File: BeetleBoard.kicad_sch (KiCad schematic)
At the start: 1 part, among them U1 XIAO-ESP32-C6-SMD

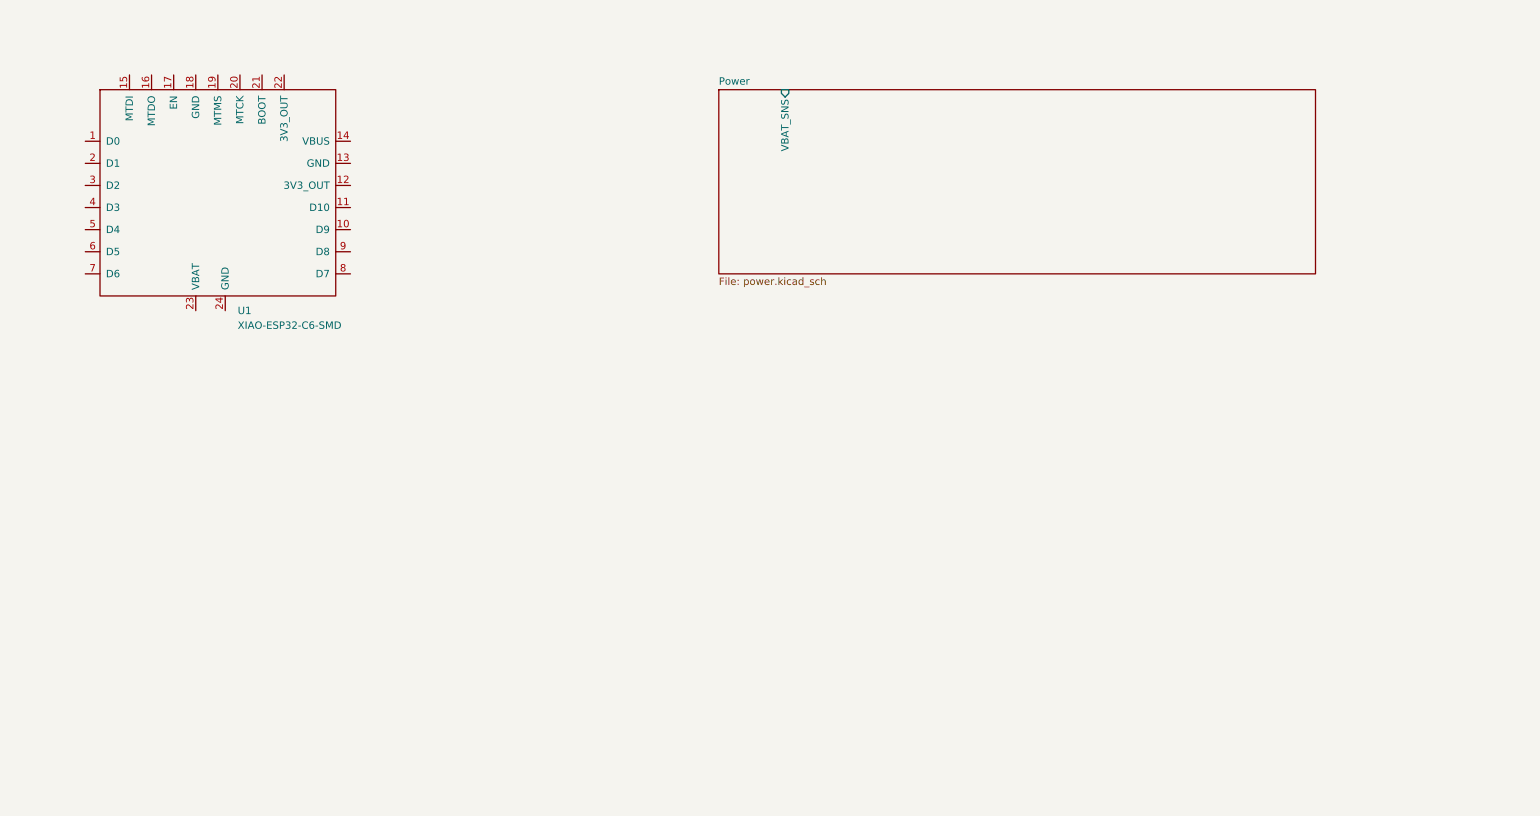
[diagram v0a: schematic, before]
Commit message: add ESC Ports
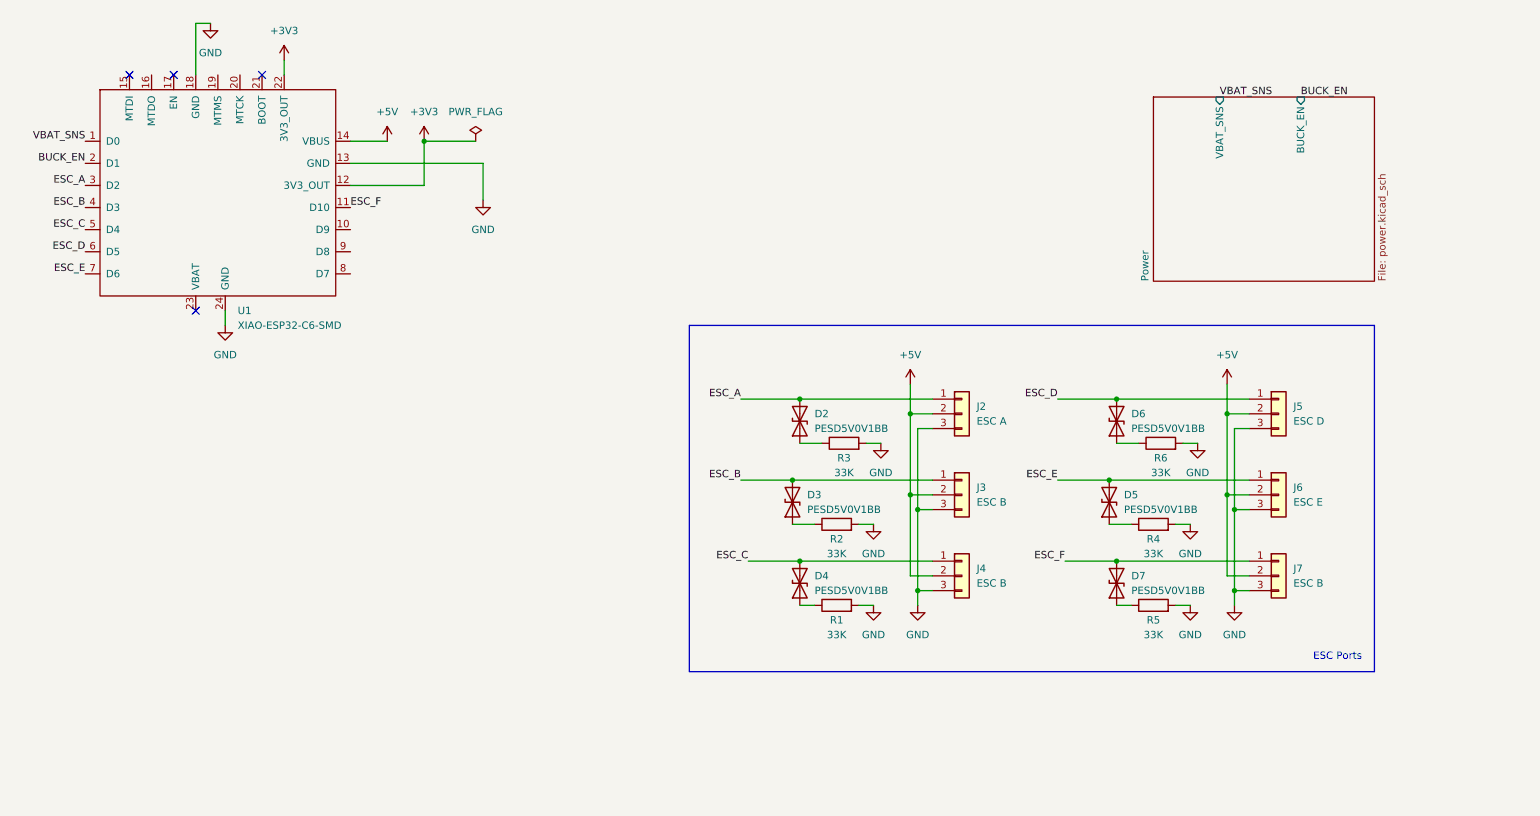
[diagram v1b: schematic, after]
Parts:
- added D2, D3, D4, D5, D6, D7: PESD5V0V1BB, symbol Device:D_TVS
- added J2: ESC A, symbol Connector_Generic:Conn_01x03
- added J3, J4, J7: ESC B, symbol Connector_Generic:Conn_01x03
- added J5: ESC D, symbol Connector_Generic:Conn_01x03
- added J6: ESC E, symbol Connector_Generic:Conn_01x03
- added R1, R2, R3, R4, R5, R6: 33K, symbol Device:R
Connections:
- net VBAT_SNS: now reaches U1.1 (D0)
- net ESC_F: now reaches U1.11 (D10)
- net ESC_F: now also D7.2 (A2), J7.1 (DShot/PWM)
- net +3V3: now reaches U1.12 (3V3_OUT)
- net +3V3: now also U1.22 (3V3_OUT)
- net GND: now reaches U1.13 (GND)
- net GND: now also U1.18 (GND), U1.24 (GND), J2.3 (GND), J3.3 (GND), J4.3 (GND), J5.3 (GND), J6.3 (GND), J7.3 (GND), R1.2, R2.2, R3.2, R4.2, R5.2, R6.2
- net +5V: now reaches U1.14 (VBUS)
- net +5V: now also J2.2 (+5V), J3.2 (+5V), J4.2 (+5V), J5.2 (+5V), J6.2 (+5V), J7.2 (+5V)
- net BUCK_EN: now reaches U1.2 (D1)
- net ESC_A: now reaches U1.3 (D2)
- net ESC_A: now also D2.2 (A2), J2.1 (DShot/PWM)
- net ESC_B: now reaches U1.4 (D3)
- net ESC_B: now also D3.2 (A2), J3.1 (DShot/PWM)
- net ESC_C: now reaches U1.5 (D4)
- net ESC_C: now also D4.2 (A2), J4.1 (DShot/PWM)
- net ESC_D: now reaches U1.6 (D5)
- net ESC_D: now also D6.2 (A2), J5.1 (DShot/PWM)
- net ESC_E: now reaches U1.7 (D6)
- net ESC_E: now also D5.2 (A2), J6.1 (DShot/PWM)
- new net: D3.1 (A1), R2.1
- new net: D7.1 (A1), R5.1
- new net: D4.1 (A1), R1.1
- new net: D5.1 (A1), R4.1
- new net: D2.1 (A1), R3.1
- new net: D6.1 (A1), R6.1
- no-connect marks 0 -> 4
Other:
- sheet Power ports: added BUCK_EN; removed none
- note added: "ESC Ports"
- company: (none) -> avycado13
- title: (none) -> BeetleBoard

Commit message: add IMU
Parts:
- added C10: 0.1uF, symbol Device:C
- added C9: 2.2nF, symbol Device:C
- added U3: MPU-6050, Sensor_Motion:InvenSense_QFN-24_4x4mm_P0.5mm, symbol Sensor_Motion:MPU-6050
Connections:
- net +3V3: now also U3.13 (VDD), U3.8 (VLOGIC)
- net ESC_C: now also U1.16 (MTDO); no longer U1.5 (D4)
- net ESC_D: now also U1.9 (D8); no longer U1.6 (D5)
- net ESC_E: now also U1.10 (D9); no longer U1.7 (D6)
- net GND: now also C10.2, C9.2, U3.1 (CLKIN), U3.11 (FSYNC), U3.18 (GND), U3.9 (AD0)
- net MPU_INT: now reaches U1.15 (MTDI)
- net MPU_INT: now also U3.12 (INT)
- net XIAO_RX: now reaches U1.8 (D7)
- new net: C9.1, U3.20 (CPOUT)
- new net: C10.1, U3.10 (REGOUT)
- new net SCL: U1.6 (D5), U3.23 (SCL)
- new net SDA: U1.5 (D4), U3.24 (SDA)
- new net XIAO_TX: U1.7 (D6)
- no-connect marks 4 -> 7

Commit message: fix power distrubution
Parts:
- J7: value ESC B -> ESC F
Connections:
- net +5V: no longer J6.2 (+5V), J7.2 (+5V)
- new net: J6.2 (+5V), J7.2 (+5V)
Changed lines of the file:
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@@
 	(rectangle
 		(start 135.89 71.12)
-		(end 254 130.81)
+		(end 279.4 130.81)
 		(stroke
 			(width 0)
@@
 	(text "ESC Ports"
 		(exclude_from_sim no)
-		(at 247.65 128.27 0)
+		(at 271.78 128.27 0)
 		(effects
 			(font
@@
 	(junction
 		(at 153.67 97.79)
-		(diameter 0)
-		(color 0 0 0 0)
-	)
-	(junction
-		(at 228.6 86.36)
 		(diameter 0)
 		(color 0 0 0 0)
@@
 	(wire
 		(pts
-			(xy 228.6 86.36) (xy 228.6 100.33)
+			(xy 214.63 100.33) (xy 228.6 100.33)
 		)
 		(stroke
@@
 			)
 		)
-		(property "Value" "ESC B"
+		(property "Value" "ESC F"
 			(at 240.03 115.5699 0)
 			(show_name no)

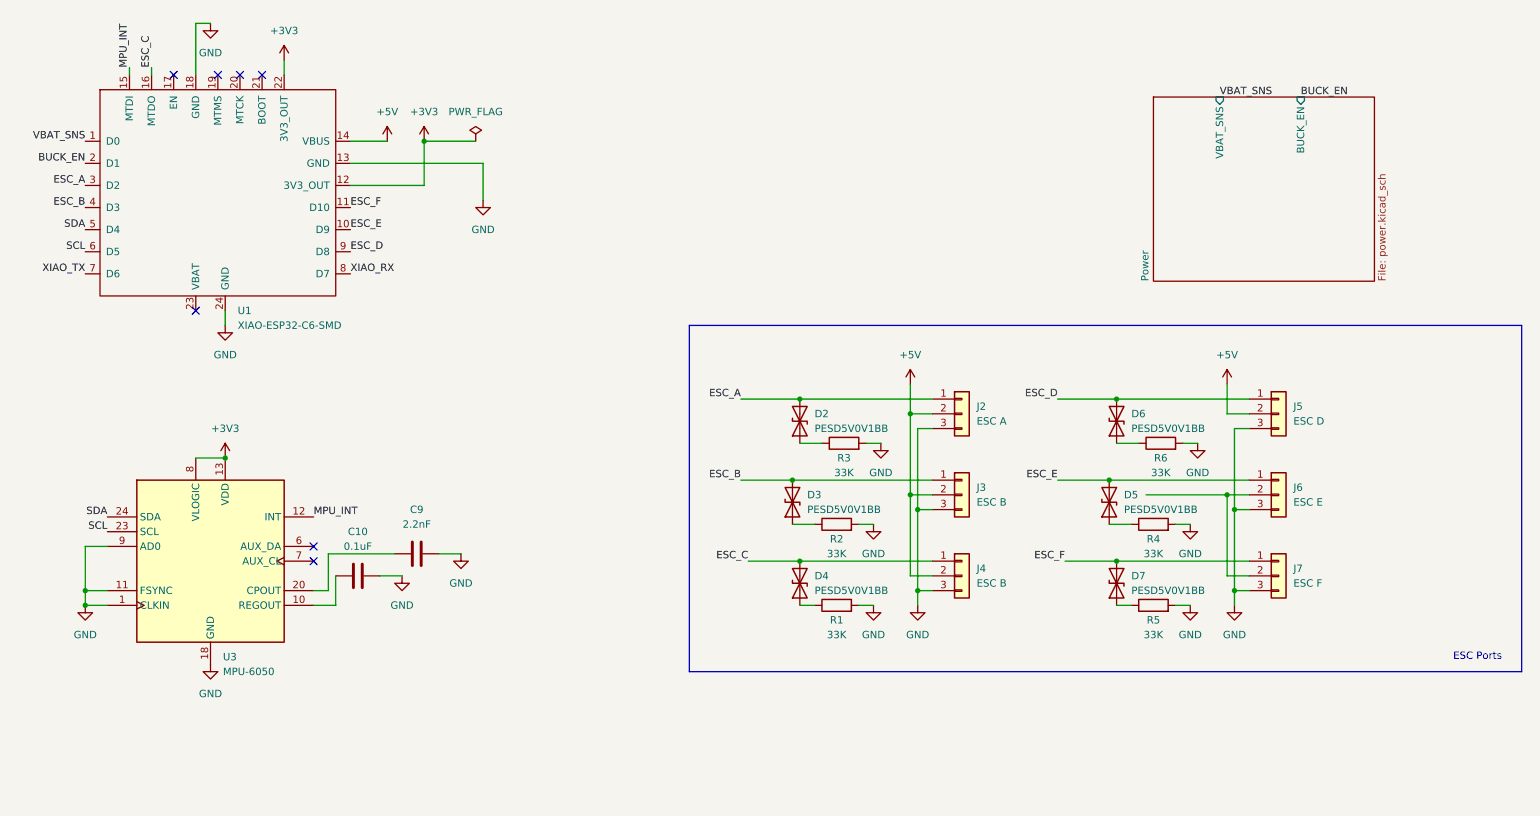
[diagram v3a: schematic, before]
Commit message: add revised IMU
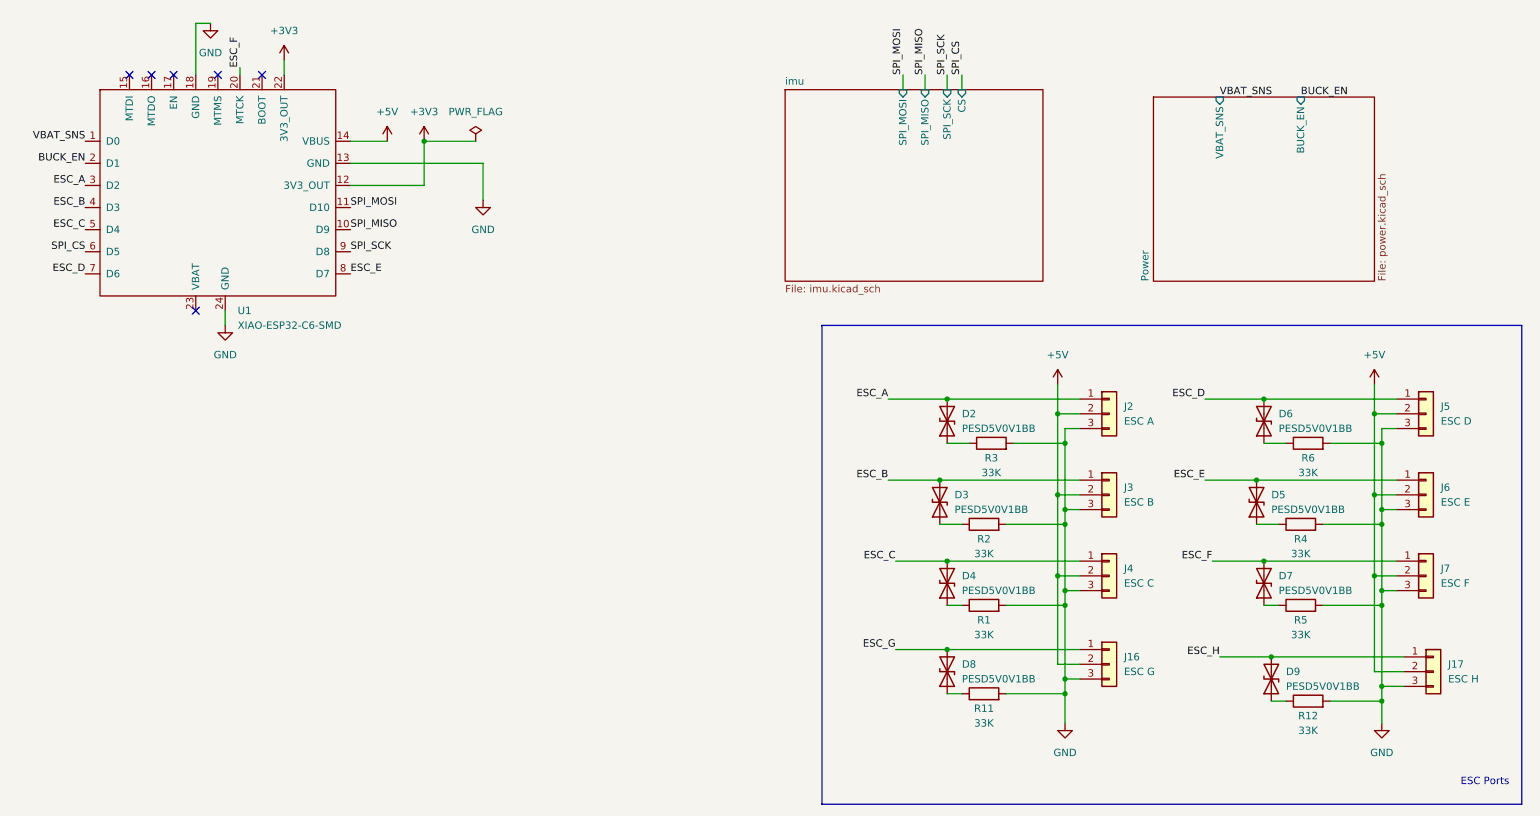
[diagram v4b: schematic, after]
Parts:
- removed C10: 0.1uF, symbol Device:C
- removed C9: 2.2nF, symbol Device:C
- removed U3: MPU-6050, Sensor_Motion:InvenSense_QFN-24_4x4mm_P0.5mm, symbol Sensor_Motion:MPU-6050
- added D8, D9: PESD5V0V1BB, symbol Device:D_TVS
- added J16: ESC G, symbol Connector_Generic:Conn_01x03
- added J17: ESC H, symbol Connector_Generic:Conn_01x03
- added R11, R12: 33K, symbol Device:R
- J4: value ESC B -> ESC C
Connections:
- net SDA is gone; now on net ESC_C: U1.5 (D4)
- net XIAO_RX is gone; now on net ESC_E: U1.8 (D7)
- net XIAO_TX is gone; now on net ESC_D: U1.7 (D6)
- net +5V: now also J6.2 (+5V), J7.2 (+5V), J16.2 (+5V), J17.2 (+5V)
- net ESC_C: no longer U1.16 (MTDO)
- net ESC_D: no longer U1.9 (D8)
- net ESC_E: no longer U1.10 (D9)
- net ESC_F: now also U1.20 (MTCK); no longer U1.11 (D10)
- net GND: now also J16.3 (GND), J17.3 (GND), R11.2, R12.2
- net MPU_INT: no longer names the net of U1.15 (MTDI)
- net SCL renamed SPI_CS
- new net: D8.1 (A1), R11.1
- new net: D9.1 (A1), R12.1
- new net ESC_G: D8.2 (A2), J16.1 (DShot/PWM)
- new net ESC_H: D9.2 (A2), J17.1 (DShot/PWM)
- new net SPI_MISO: U1.10 (D9)
- new net SPI_MOSI: U1.11 (D10)
- new net SPI_SCK: U1.9 (D8)
- no-connect marks 7 -> 6
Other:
- added sheet imu (imu.kicad_sch)
- moved on the sheet: D2, D3, D4, D5, D6, D7, J2, J3, J4, J5, J6, J7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

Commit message: add ELRS Reciever and clean up some stuff
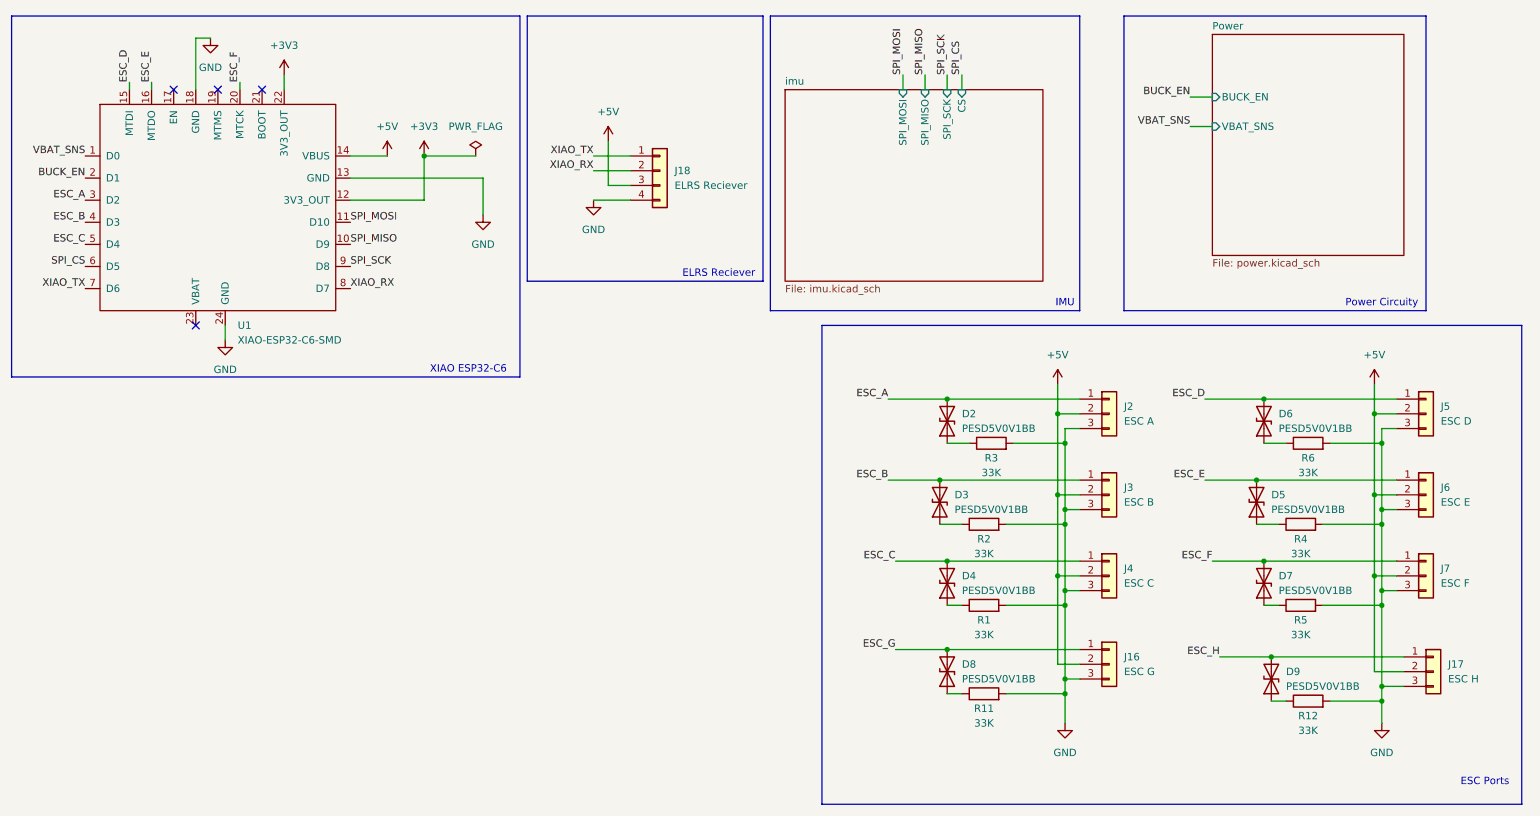
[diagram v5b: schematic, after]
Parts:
- added J18: ELRS Reciever, symbol Connector_Generic:Conn_01x04
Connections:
- net +5V: now also J18.3 (Pin_3)
- net ESC_D: now also U1.15 (MTDI); no longer U1.7 (D6)
- net ESC_E: now also U1.16 (MTDO); no longer U1.8 (D7)
- net GND: now also J18.4 (Pin_4)
- new net XIAO_RX: J18.2 (Pin_2), U1.8 (D7)
- new net XIAO_TX: J18.1 (Pin_1), U1.7 (D6)
- no-connect marks 6 -> 4
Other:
- note added: "ELRS Reciever"
- note added: "IMU"
- note added: "Power Circuity"
- note added: "XIAO ESP32-C6"
- moved on the sheet: U1

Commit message: clean up schematics and start pcb
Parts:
- D2, D3, D4, D5, D6, D7, D8, D9: footprint (none) -> Diode_SMD:D_SOD-323
- J16, J17, J2, J3, J4, J5, J6, J7: footprint (none) -> Connector_PinHeader_2.54mm:PinHeader_1x03_P2.54mm_Vertical
- J18: footprint (none) -> footprints:BetaFPV_ELRS_Lite
- R1, R11, R12, R2, R3, R4, R5, R6: footprint (none) -> Resistor_SMD:R_0805_2012Metric_Pad1.20x1.40mm_HandSolder
- U1: footprint Seeed_Studio_XIAO_Series:XIAO-ESP32-C6-SMD -> Seeed Studio XIAO Series Library:XIAO-ESP32-C6-SMD
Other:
- moved on the sheet: J18, U1

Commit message: Thicken power traces and some cleanup
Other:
- sheet Power: file power.kicad_sch -> subsheets/power.kicad_sch
- sheet imu: file imu.kicad_sch -> subsheets/imu.kicad_sch
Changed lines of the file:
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@@
 			)
 		)
-		(property "Sheetfile" "power.kicad_sch"
+		(property "Sheetfile" "subsheets/power.kicad_sch"
 			(at 242.57 60.9096 0)
 			(show_name no)
@@
 			)
 		)
-		(property "Sheetfile" "imu.kicad_sch"
+		(property "Sheetfile" "subsheets/imu.kicad_sch"
 			(at 172.72 65.3546 0)
 			(show_name no)
